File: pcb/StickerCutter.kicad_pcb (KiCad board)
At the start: 2 copper layers, 111.1 x 164.5 mm, 27 parts, among them J1 24V, J3 Line Sensor, J4 Paper Sensor, J5 ENC_0, J6 ENC_1, SW1 F1, SW2 F2, SW3 Forward, SW4 Backward, SW5 Left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

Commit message: Fixed forgotten routes
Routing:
- net +5V: track 208.4 -> 270.9 mm
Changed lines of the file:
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@@
   (segment (start 69.215 46.609) (end 71.6153 46.609) (width 1) (layer "B.Cu") (net 1))
   (segment (start 40.64 104.648) (end 42.672 106.68) (width 1) (layer "B.Cu") (net 1))
+  (segment (start 51.816 76.708) (end 80.772 76.708) (width 1) (layer "F.Cu") (net 12))
   (segment (start 105.156 84.328) (end 109.728 79.756) (width 1) (layer "F.Cu") (net 12))
+  (segment (start 44.735 96.124) (end 42.56 96.124) (width 1) (layer "F.Cu") (net 12))
   (segment (start 109.728 75.692) (end 114.3 71.12) (width 1) (layer "F.Cu") (net 12))
+  (segment (start 49.773 80.069) (end 49.773 78.751) (width 1) (layer "F.Cu") (net 12))
+  (segment (start 80.772 76.708) (end 82.804 78.74) (width 1) (layer "F.Cu") (net 12))
   (segment (start 85.344 84.328) (end 105.156 84.328) (width 1) (layer "F.Cu") (net 12))
   (segment (start 109.728 79.756) (end 109.728 75.692) (width 1) (layer "F.Cu") (net 12))
+  (segment (start 82.804 78.74) (end 82.804 80.058) (width 1) (layer "F.Cu") (net 12))
+  (segment (start 42.672 115.824) (end 44.704 115.824) (width 1) (layer "F.Cu") (net 12))
+  (segment (start 42.56 96.124) (end 41.148 97.536) (width 1) (layer "F.Cu") (net 12))
+  (segment (start 41.148 97.536) (end 41.148 114.3) (width 1) (layer "F.Cu") (net 12))
   (segment (start 114.3 71.12) (end 115.316 71.12) (width 1) (layer "F.Cu") (net 12))
+  (segment (start 49.773 78.751) (end 51.816 76.708) (width 1) (layer "F.Cu") (net 12))
+  (segment (start 41.148 114.3) (end 42.672 115.824) (width 1) (layer "F.Cu") (net 12))
+  (segment (start 82.804 80.058) (end 82.793 80.069) (width 1) (layer "F.Cu") (net 12))
   (segment (start 129.032 76.708) (end 129.032 82.296) (width 1.5) (layer "B.Cu") (net 12))
   (segment (start 130.556 75.184) (end 129.032 76.708) (width 1.5) (layer "B.Cu") (net 12))

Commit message: Added buttons, improved manual mode
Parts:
- SW3: value Forward -> In
- SW4: value Backward -> Out
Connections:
- U1 pad 1: /Backward -> /Out
- U1 pad 6: /Forward -> /In
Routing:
- net /In: track 0.00 -> 78.1 mm
- net /Forward: track 78.1 -> 0.00 mm

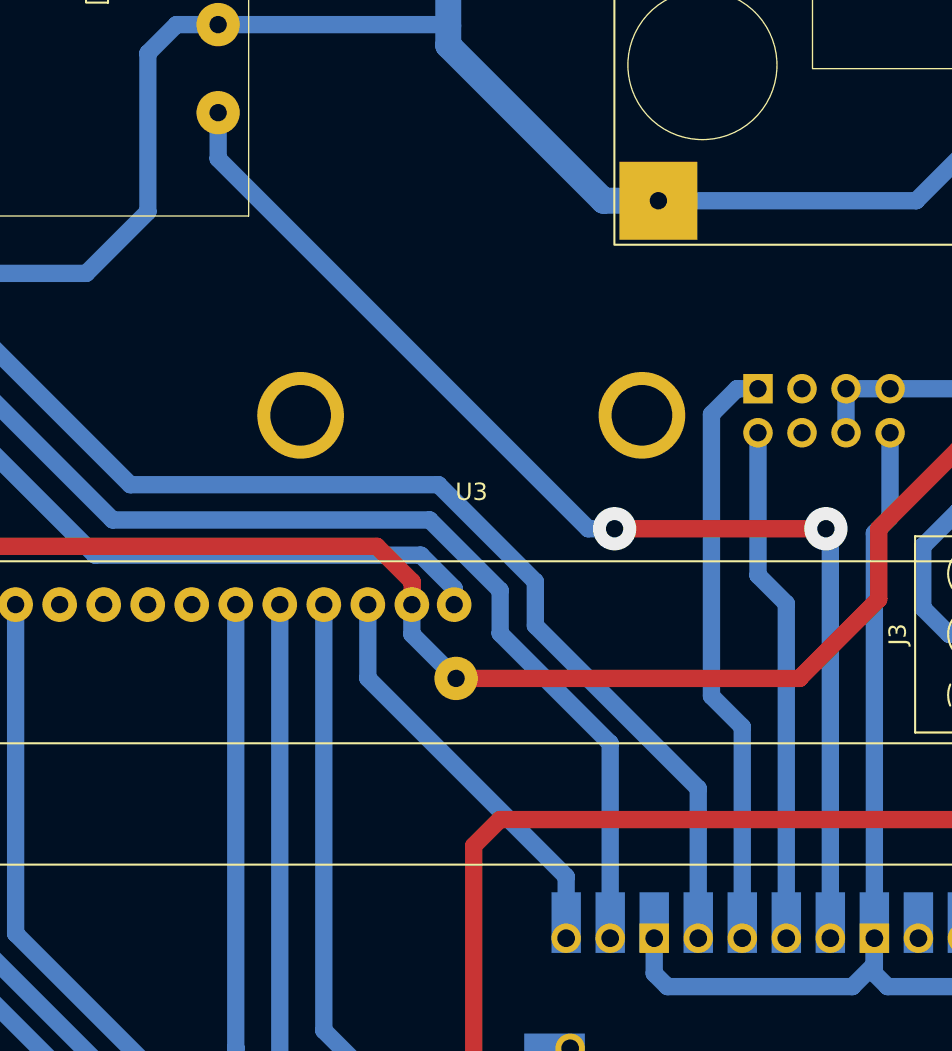
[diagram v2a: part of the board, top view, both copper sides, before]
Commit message: Moved pwm chans to fit pwm hw pairs in RP2040
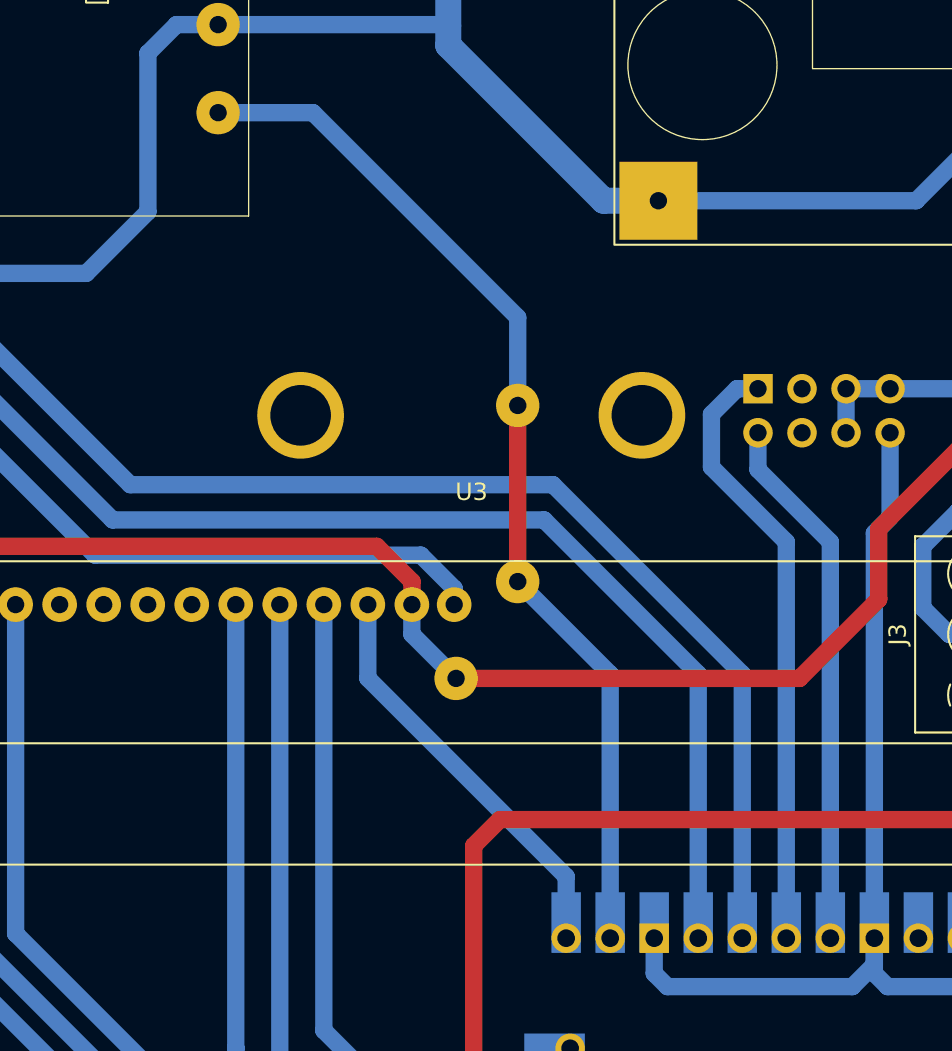
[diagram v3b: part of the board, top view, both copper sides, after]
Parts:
- added ?: , , F.Cu at (88.9, 68.6)
- added ?: , , F.Cu at (88.9, 78.7)
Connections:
- U1 pad 22: /Servo_0_RPWM -> /Knife
- U1 pad 24: /Servo_0_LPWM -> /Servo_0_RPWM
- U1 pad 25: /Servo_1_RPWM -> /Servo_0_LPWM
- U1 pad 26: /Servo_1_LPWM -> /Servo_1_RPWM
- U1 pad 27: /Knife -> /Servo_1_LPWM
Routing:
- net /Knife: track 70.3 -> 60.2 mm, vias 2 -> 0
- net /Servo_0_RPWM: track 75.3 -> 81.3 mm
- net /Servo_0_LPWM: track 88.0 -> 93.3 mm
- net /Servo_1_RPWM: track 34.6 -> 35.7 mm
- net /Servo_1_LPWM: track 30.2 -> 30.9 mm
